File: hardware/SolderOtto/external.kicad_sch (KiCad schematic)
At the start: 13 parts, among them J901 Conn_01x08

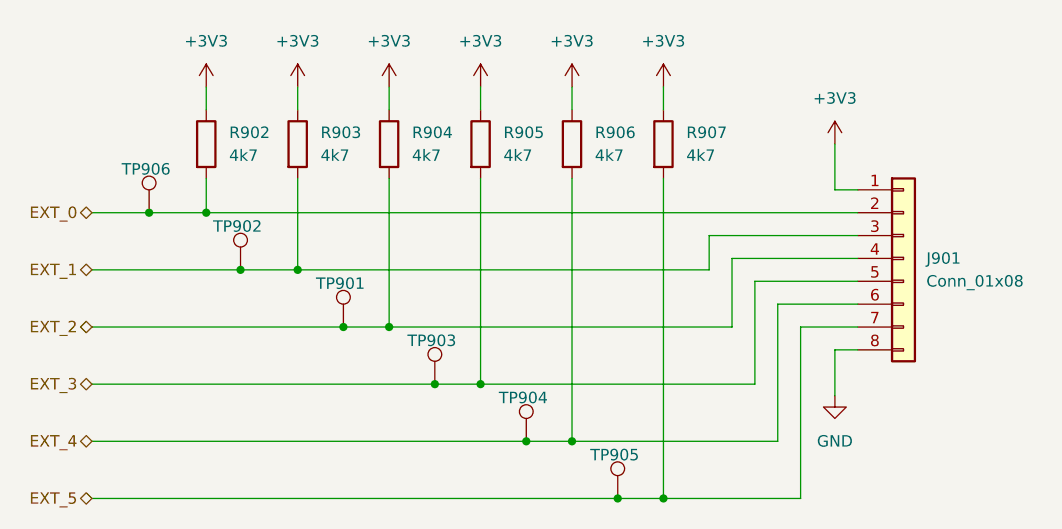
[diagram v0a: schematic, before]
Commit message: create adapter to enclosure for display
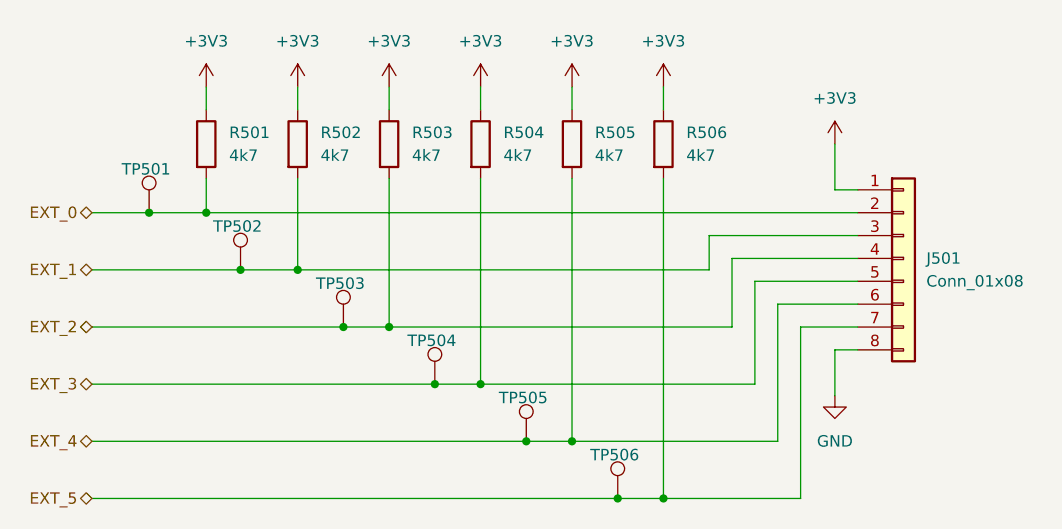
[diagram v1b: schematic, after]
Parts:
- renumbered J901 to J501, R902 to R501, R903 to R502, R904 to R503, R905 to R504, R906 to R505, R907 to R506, TP906 to TP501, TP902 to TP502, TP901 to TP503, TP903 to TP504, TP904 to TP505, TP905 to TP506
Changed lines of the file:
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@@
 		(dnp no)
 		(fields_autoplaced yes)
-		(property "Reference" "R907"
+		(property "Reference" "R506"
 			(at 135.89 40.6399 0)
 			(effects
@@
 			(project "SolderOtto"
 				(path "/04e99464-bf33-4a4f-8397-d26b5ec904f3/cd418f0e-1056-4277-8df0-d16a810128a6"
-					(reference "R907")
+					(reference "R506")
 					(unit 1)
 				)
@@
 		(dnp no)
 		(fields_autoplaced yes)
-		(property "Reference" "#PWR0909"
+		(property "Reference" "#PWR0505"
 			(at 123.19 39.37 0)
 			(effects
@@
 			(project "SolderOtto"
 				(path "/04e99464-bf33-4a4f-8397-d26b5ec904f3/cd418f0e-1056-4277-8df0-d16a810128a6"
-					(reference "#PWR0909")
+					(reference "#PWR0505")
 					(unit 1)
 				)
@@
 		(dnp no)
 		(fields_autoplaced yes)
-		(property "Reference" "R906"
+		(property "Reference" "R505"
 			(at 125.73 40.6399 0)
 			(effects
@@
 			(project "SolderOtto"
 				(path "/04e99464-bf33-4a4f-8397-d26b5ec904f3/cd418f0e-1056-4277-8df0-d16a810128a6"
-					(reference "R906")
+					(reference "R505")
 					(unit 1)
 				)
@@
 		(dnp no)
 		(fields_autoplaced yes)
-		(property "Reference" "R902"
+		(property "Reference" "R501"
 			(at 85.09 40.6399 0)
 			(effects
@@
 			(project "SolderOtto"
 				(path "/04e99464-bf33-4a4f-8397-d26b5ec904f3/cd418f0e-1056-4277-8df0-d16a810128a6"
-					(reference "R902")
+					(reference "R501")
 					(unit 1)
 				)
@@
 		(dnp no)
 		(fields_autoplaced yes)
-		(property "Reference" "#PWR0905"
+		(property "Reference" "#PWR0501"
 			(at 82.55 39.37 0)
 			(effects
@@
 			(project "SolderOtto"
 				(path "/04e99464-bf33-4a4f-8397-d26b5ec904f3/cd418f0e-1056-4277-8df0-d16a810128a6"
-					(reference "#PWR0905")
+					(reference "#PWR0501")
 					(unit 1)
 				)
@@
 		(on_board yes)
 		(dnp no)
-		(property "Reference" "TP903"
+		(property "Reference" "TP504"
 			(at 104.902 63.754 0)
 			(effects
@@
 			(project "SolderOtto"
 				(path "/04e99464-bf33-4a4f-8397-d26b5ec904f3/cd418f0e-1056-4277-8df0-d16a810128a6"
-					(reference "TP903")
+					(reference "TP504")
 					(unit 1)
 				)
@@
 		(on_board yes)
 		(dnp no)
-		(property "Reference" "TP902"
+		(property "Reference" "TP502"
 			(at 83.312 51.054 0)
 			(effects
@@
 			(project "SolderOtto"
 				(path "/04e99464-bf33-4a4f-8397-d26b5ec904f3/cd418f0e-1056-4277-8df0-d16a810128a6"
-					(reference "TP902")
+					(reference "TP502")
 					(unit 1)
 				)
@@
 		(on_board yes)
 		(dnp no)
-		(property "Reference" "TP905"
+		(property "Reference" "TP506"
 			(at 125.222 76.454 0)
 			(effects
@@
 			(project "SolderOtto"
 				(path "/04e99464-bf33-4a4f-8397-d26b5ec904f3/cd418f0e-1056-4277-8df0-d16a810128a6"
-					(reference "TP905")
+					(reference "TP506")
 					(unit 1)
 				)
@@
 		(on_board yes)
 		(dnp no)
-		(property "Reference" "TP906"
+		(property "Reference" "TP501"
 			(at 73.152 44.704 0)
 			(effects
@@
 			(project "SolderOtto"
 				(path "/04e99464-bf33-4a4f-8397-d26b5ec904f3/cd418f0e-1056-4277-8df0-d16a810128a6"
-					(reference "TP906")
+					(reference "TP501")
 					(unit 1)
 				)
@@
 		(dnp no)
 		(fields_autoplaced yes)
-		(property "Reference" "#PWR0907"
+		(property "Reference" "#PWR0503"
 			(at 102.87 39.37 0)
 			(effects
@@
 			(project "SolderOtto"
 				(path "/04e99464-bf33-4a4f-8397-d26b5ec904f3/cd418f0e-1056-4277-8df0-d16a810128a6"
-					(reference "#PWR0907")
+					(reference "#PWR0503")
 					(unit 1)
 				)
@@
 		(dnp no)
 		(fields_autoplaced yes)
-		(property "Reference" "#PWR0908"
+		(property "Reference" "#PWR0504"
 			(at 113.03 39.37 0)
 			(effects
@@
 			(project "SolderOtto"
 				(path "/04e99464-bf33-4a4f-8397-d26b5ec904f3/cd418f0e-1056-4277-8df0-d16a810128a6"
-					(reference "#PWR0908")
+					(reference "#PWR0504")
 					(unit 1)
 				)
@@
 		(dnp no)
 		(fields_autoplaced yes)
-		(property "Reference" "#PWR0906"
+		(property "Reference" "#PWR0502"
 			(at 92.71 39.37 0)
 			(effects
@@
 			(project "SolderOtto"
 				(path "/04e99464-bf33-4a4f-8397-d26b5ec904f3/cd418f0e-1056-4277-8df0-d16a810128a6"
-					(reference "#PWR0906")
+					(reference "#PWR0502")
 					(unit 1)
 				)
@@
 		(dnp no)
 		(fields_autoplaced yes)
-		(property "Reference" "#PWR0911"
+		(property "Reference" "#PWR0507"
 			(at 152.4 45.72 0)
 			(effects
@@
 			(project "SolderOtto"
 				(path "/04e99464-bf33-4a4f-8397-d26b5ec904f3/cd418f0e-1056-4277-8df0-d16a810128a6"
-					(reference "#PWR0911")
+					(reference "#PWR0507")
 					(unit 1)
 				)
@@
 		(on_board yes)
 		(dnp no)
-		(property "Reference" "TP901"
+		(property "Reference" "TP503"
 			(at 94.742 57.404 0)
 			(effects
@@
 			(project "SolderOtto"
 				(path "/04e99464-bf33-4a4f-8397-d26b5ec904f3/cd418f0e-1056-4277-8df0-d16a810128a6"
-					(reference "TP901")
+					(reference "TP503")
 					(unit 1)
 				)
@@
 		(dnp no)
 		(fields_autoplaced yes)
-		(property "Reference" "J901"
+		(property "Reference" "J501"
 			(at 162.56 54.6099 0)
 			(effects
@@
 			(project ""
 				(path "/04e99464-bf33-4a4f-8397-d26b5ec904f3/cd418f0e-1056-4277-8df0-d16a810128a6"
-					(reference "J901")
+					(reference "J501")
 					(unit 1)
 				)
@@
 		(dnp no)
 		(fields_autoplaced yes)
-		(property "Reference" "R903"
+		(property "Reference" "R502"
 			(at 95.25 40.6399 0)
 			(effects
@@
 			(project "SolderOtto"
 				(path "/04e99464-bf33-4a4f-8397-d26b5ec904f3/cd418f0e-1056-4277-8df0-d16a810128a6"
-					(reference "R903")
+					(reference "R502")
 					(unit 1)
 				)
@@
 		(dnp no)
 		(fields_autoplaced yes)
-		(property "Reference" "R905"
+		(property "Reference" "R504"
 			(at 115.57 40.6399 0)
 			(effects
@@
 			(project "SolderOtto"
 				(path "/04e99464-bf33-4a4f-8397-d26b5ec904f3/cd418f0e-1056-4277-8df0-d16a810128a6"
-					(reference "R905")
+					(reference "R504")
 					(unit 1)
 				)
@@
 		(dnp no)
 		(fields_autoplaced yes)
-		(property "Reference" "R904"
+		(property "Reference" "R503"
 			(at 105.41 40.6399 0)
 			(effects
@@
 			(project "SolderOtto"
 				(path "/04e99464-bf33-4a4f-8397-d26b5ec904f3/cd418f0e-1056-4277-8df0-d16a810128a6"
-					(reference "R904")
+					(reference "R503")
 					(unit 1)
 				)
@@
 		(dnp no)
 		(fields_autoplaced yes)
-		(property "Reference" "#PWR0910"
+		(property "Reference" "#PWR0506"
 			(at 133.35 39.37 0)
 			(effects
@@
 			(project "SolderOtto"
 				(path "/04e99464-bf33-4a4f-8397-d26b5ec904f3/cd418f0e-1056-4277-8df0-d16a810128a6"
-					(reference "#PWR0910")
+					(reference "#PWR0506")
 					(unit 1)
 				)
@@
 		(on_board yes)
 		(dnp no)
-		(property "Reference" "TP904"
+		(property "Reference" "TP505"
 			(at 115.062 70.104 0)
 			(effects
@@
 			(project "SolderOtto"
 				(path "/04e99464-bf33-4a4f-8397-d26b5ec904f3/cd418f0e-1056-4277-8df0-d16a810128a6"
-					(reference "TP904")
+					(reference "TP505")
 					(unit 1)
 				)
@@
 		(dnp no)
 		(fields_autoplaced yes)
-		(property "Reference" "#PWR0912"
+		(property "Reference" "#PWR0508"
 			(at 152.4 76.2 0)
 			(effects
@@
 			(project "SolderOtto"
 				(path "/04e99464-bf33-4a4f-8397-d26b5ec904f3/cd418f0e-1056-4277-8df0-d16a810128a6"
-					(reference "#PWR0912")
-					(unit 1)
-				)
+					(reference "#PWR0508")
+					(unit 1)
+				)

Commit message: save work
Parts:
- TP501: value ZCD -> EXT0
- TP502: value ZCD -> EXT1
- TP503: value ZCD -> EXT2
- TP504: value ZCD -> EXT3
- TP505: value ZCD -> EXT4
- TP506: value ZCD -> EXT5
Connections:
- net EXT_3: now also J501.6 (Pin_6); no longer J501.5 (Pin_5)
- net EXT_4: now also J501.7 (Pin_7); no longer J501.6 (Pin_6)
- net EXT_5: now also J501.8 (Pin_8); no longer J501.7 (Pin_7)
- net GND: now also J501.5 (Pin_5); no longer J501.8 (Pin_8)
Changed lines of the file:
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@@
 	(wire
 		(pts
-			(xy 123.19 74.93) (xy 146.05 74.93)
-		)
-		(stroke
-			(width 0)
-			(type default)
-		)
-	)
-	(wire
-		(pts
-			(xy 152.4 69.85) (xy 152.4 64.77)
+			(xy 152.4 64.77) (xy 154.94 64.77)
+		)
+		(stroke
+			(width 0)
+			(type default)
+		)
+	)
+	(wire
+		(pts
+			(xy 123.19 74.93) (xy 149.86 74.93)
+		)
+		(stroke
+			(width 0)
+			(type default)
+		)
+	)
+	(wire
+		(pts
+			(xy 143.51 62.23) (xy 143.51 57.15)
 		)
 		(stroke
@@
 	(wire
 		(pts
-			(xy 148.59 81.28) (xy 148.59 62.23)
-		)
-		(stroke
-			(width 0)
-			(type default)
-		)
-	)
-	(wire
-		(pts
 			(xy 102.87 62.23) (xy 140.97 62.23)
 		)
@@
 	(wire
 		(pts
-			(xy 143.51 68.58) (xy 143.51 57.15)
+			(xy 147.32 68.58) (xy 147.32 59.69)
 		)
 		(stroke
@@
 	(wire
 		(pts
-			(xy 146.05 59.69) (xy 146.05 74.93)
-		)
-		(stroke
-			(width 0)
-			(type default)
-		)
-	)
-	(wire
-		(pts
-			(xy 133.35 81.28) (xy 148.59 81.28)
+			(xy 152.4 81.28) (xy 152.4 64.77)
+		)
+		(stroke
+			(width 0)
+			(type default)
+		)
+	)
+	(wire
+		(pts
+			(xy 149.86 62.23) (xy 149.86 74.93)
+		)
+		(stroke
+			(width 0)
+			(type default)
+		)
+	)
+	(wire
+		(pts
+			(xy 133.35 81.28) (xy 152.4 81.28)
 		)
 		(stroke
@@
 	(wire
 		(pts
-			(xy 152.4 64.77) (xy 154.94 64.77)
-		)
-		(stroke
-			(width 0)
-			(type default)
-		)
-	)
-	(wire
-		(pts
-			(xy 154.94 59.69) (xy 146.05 59.69)
+			(xy 143.51 57.15) (xy 154.94 57.15)
+		)
+		(stroke
+			(width 0)
+			(type default)
+		)
+	)
+	(wire
+		(pts
+			(xy 154.94 62.23) (xy 149.86 62.23)
 		)
 		(stroke
@@
 	(wire
 		(pts
-			(xy 113.03 68.58) (xy 143.51 68.58)
+			(xy 113.03 68.58) (xy 147.32 68.58)
 		)
 		(stroke
@@
 	(wire
 		(pts
-			(xy 148.59 62.23) (xy 154.94 62.23)
-		)
-		(stroke
-			(width 0)
-			(type default)
-		)
-	)
-	(wire
-		(pts
 			(xy 133.35 81.28) (xy 133.35 45.72)
 		)
@@
 	(wire
 		(pts
-			(xy 143.51 57.15) (xy 154.94 57.15)
+			(xy 147.32 59.69) (xy 154.94 59.69)
 		)
 		(stroke
@@
 			)
 		)
-		(property "Value" "ZCD"
+		(property "Value" "EXT3"
 			(at 110.49 66.5479 0)
 			(effects
@@
 			)
 		)
-		(property "Value" "ZCD"
+		(property "Value" "EXT1"
 			(at 88.9 53.8479 0)
 			(effects
@@
 			)
 		)
-		(property "Value" "ZCD"
+		(property "Value" "EXT5"
 			(at 130.81 79.2479 0)
 			(effects
@@
 			)
 		)
-		(property "Value" "ZCD"
+		(property "Value" "EXT0"
 			(at 78.74 47.4979 0)
 			(effects
@@
 			)
 		)
-		(property "Value" "ZCD"
+		(property "Value" "EXT2"
 			(at 100.33 60.1979 0)
 			(effects
@@
 			)
 		)
-		(property "Value" "ZCD"
+		(property "Value" "EXT4"
 			(at 120.65 72.8979 0)
 			(effects
@@
 	(symbol
 		(lib_id "power:GND")
-		(at 152.4 69.85 0)
+		(at 143.51 62.23 0)
 		(unit 1)
 		(exclude_from_sim no)
@@
 		(fields_autoplaced yes)
 		(property "Reference" "#PWR0508"
-			(at 152.4 76.2 0)
+			(at 143.51 68.58 0)
 			(effects
 				(font
@@
 		)
 		(property "Value" "GND"
-			(at 152.4 74.93 0)
+			(at 143.51 67.31 0)
 			(effects
 				(font
@@
 		)
 		(property "Footprint" ""
-			(at 152.4 69.85 0)
+			(at 143.51 62.23 0)
 			(effects
 				(font
@@
 		)
 		(property "Datasheet" ""
-			(at 152.4 69.85 0)
+			(at 143.51 62.23 0)
 			(effects
 				(font
@@
 		)
 		(property "Description" "Power symbol creates a global label with name \"GND\" , ground"
-			(at 152.4 69.85 0)
-			(effects
-				(font
+			(at 143.51 62.23 0)
+			(effects
+				(font

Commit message: save work
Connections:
- net EXT_0: now also J501.8 (Pin_8), R506.2, TP506.1; no longer J501.2 (Pin_2), R501.2, TP501.1
- net EXT_1: now also J501.7 (Pin_7), R505.2, TP505.1; no longer J501.3 (Pin_3), R502.2, TP502.1
- net EXT_2: now also J501.6 (Pin_6), R504.2, TP504.1; no longer J501.4 (Pin_4), R503.2, TP503.1
- net EXT_3: now also J501.4 (Pin_4), R503.2, TP503.1; no longer J501.6 (Pin_6), R504.2, TP504.1
- net EXT_4: now also J501.3 (Pin_3), R502.2, TP502.1; no longer J501.7 (Pin_7), R505.2, TP505.1
- net EXT_5: now also J501.2 (Pin_2), R501.2, TP501.1; no longer J501.8 (Pin_8), R506.2, TP506.1
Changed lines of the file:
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@@
 	(hierarchical_label "EXT_0"
+		(shape bidirectional)
+		(at 69.85 81.28 180)
+		(fields_autoplaced yes)
+		(effects
+			(font
+				(size 1.27 1.27)
+			)
+			(justify right)
+		)
+	)
+	(hierarchical_label "EXT_2"
+		(shape bidirectional)
+		(at 69.85 68.58 180)
+		(fields_autoplaced yes)
+		(effects
+			(font
+				(size 1.27 1.27)
+			)
+			(justify right)
+		)
+	)
+	(hierarchical_label "EXT_4"
+		(shape bidirectional)
+		(at 69.85 55.88 180)
+		(fields_autoplaced yes)
+		(effects
+			(font
+				(size 1.27 1.27)
+			)
+			(justify right)
+		)
+	)
+	(hierarchical_label "EXT_1"
+		(shape bidirectional)
+		(at 69.85 74.93 180)
+		(fields_autoplaced yes)
+		(effects
+			(font
+				(size 1.27 1.27)
+			)
+			(justify right)
+		)
+	)
+	(hierarchical_label "EXT_5"
 		(shape bidirectional)
 		(at 69.85 49.53 180)
@@
 		)
 	)
-	(hierarchical_label "EXT_2"
+	(hierarchical_label "EXT_3"
 		(shape bidirectional)
 		(at 69.85 62.23 180)
 		(fields_autoplaced yes)
 		(effects
-			(font
-				(size 1.27 1.27)
-			)
-			(justify right)
-		)
-	)
-	(hierarchical_label "EXT_4"
-		(shape bidirectional)
-		(at 69.85 74.93 180)
-		(fields_autoplaced yes)
-		(effects
-			(font
-				(size 1.27 1.27)
-			)
-			(justify right)
-		)
-	)
-	(hierarchical_label "EXT_1"
-		(shape bidirectional)
-		(at 69.85 55.88 180)
-		(fields_autoplaced yes)
-		(effects
-			(font
-				(size 1.27 1.27)
-			)
-			(justify right)
-		)
-	)
-	(hierarchical_label "EXT_5"
-		(shape bidirectional)
-		(at 69.85 81.28 180)
-		(fields_autoplaced yes)
-		(effects
-			(font
-				(size 1.27 1.27)
-			)
-			(justify right)
-		)
-	)
-	(hierarchical_label "EXT_3"
-		(shape bidirectional)
-		(at 69.85 68.58 180)
-		(fields_autoplaced yes)
-		(effects

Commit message: fix some part numbers
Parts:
- J501: Digikey (none) -> WM16881-ND;WM16864CT-ND;WM14964-ND;WM15189-ND
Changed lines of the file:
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@@
+			)
+		)
+		(property "Digikey" "WM16881-ND;WM16864CT-ND;WM14964-ND;WM15189-ND"
+			(at 160.02 54.61 0)
+			(effects
+				(font
+					(size 1.27 1.27)
+				)
+				(hide yes)
 			)
 		)

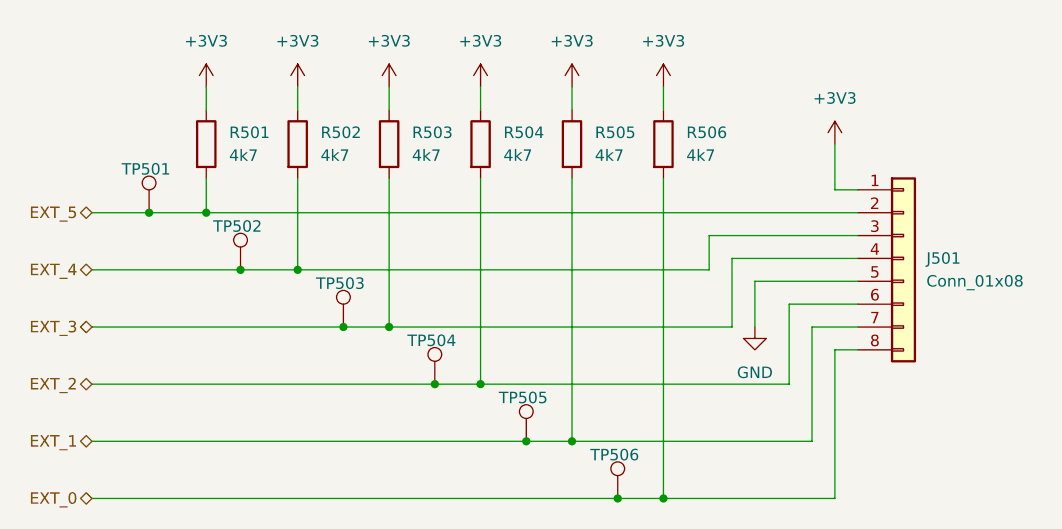
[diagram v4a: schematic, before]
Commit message: rework pcb due to not working one
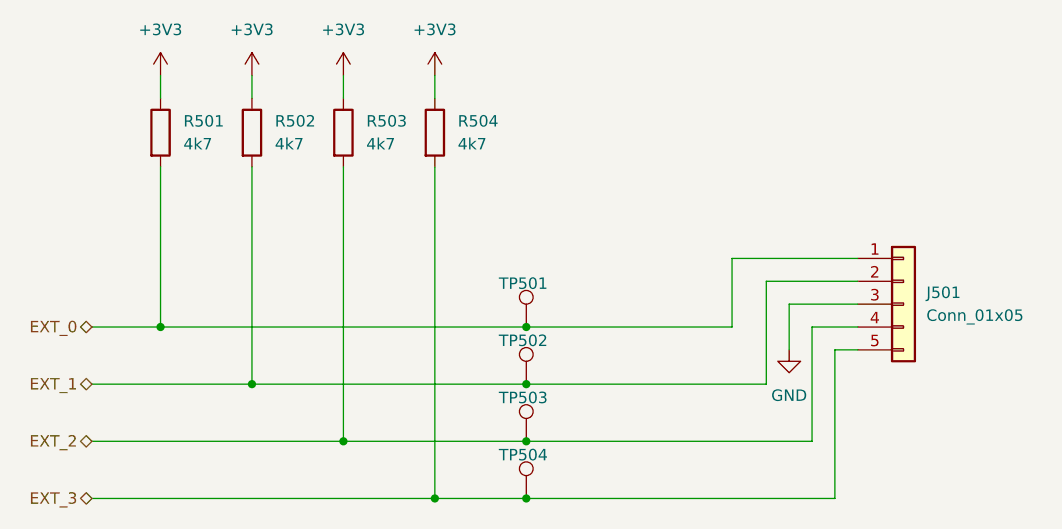
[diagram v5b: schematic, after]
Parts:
- removed J501: Conn_01x08, Connector_Molex:Molex_Nano-Fit_105310-xx08_2x04_P2.50mm_Vertical, symbol Connector_Generic:Conn_01x08
- removed R501, R502: 4k7, Resistor_SMD:R_0603_1608Metric, symbol Device:R
- removed TP501: EXT0, TestPoint:TestPoint_Keystone_5015_Micro-Minature, symbol Connector:TestPoint
- removed TP502: EXT1, TestPoint:TestPoint_Keystone_5015_Micro-Minature, symbol Connector:TestPoint
- added J501: Conn_01x05, Connector_Molex:Molex_Nano-Fit_105309-xx05_1x05_P2.50mm_Vertical, symbol Connector_Generic:Conn_01x05
- renumbered R506 to R501, R505 to R502, R504 to R503, R503 to R504, TP503 to TP501, TP504 to TP502, TP505 to TP503, TP506 to TP504
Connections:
- net EXT_0: now also TP501.1, J501.1 (Pin_1); no longer TP504.1
- net EXT_1: now also TP502.1, J501.2 (Pin_2); no longer TP503.1
- net EXT_2: now also TP503.1, J501.4 (Pin_4); no longer TP502.1
- net EXT_3: now also TP504.1, J501.5 (Pin_5); no longer TP501.1
- net GND: now also J501.3 (Pin_3)
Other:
- moved on the sheet: R501, R502, R503, R504, TP501, TP502, TP504

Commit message: rework pcb
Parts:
- J501: Digikey (none) -> WM16868-ND
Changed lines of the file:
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@@
 			)
 		)
-		(property "Datasheet" "~"
+		(property "Datasheet" "https://www.digikey.de/de/products/detail/molex/1053091105/7693149"
 			(at 160.02 59.69 0)
 			(effects
@@
 			(at 160.02 59.69 0)
 			(effects
+				(font
+					(size 1.27 1.27)
+				)
+				(hide yes)
+			)
+		)
+		(property "Digikey" "WM16868-ND"
+			(at 160.02 59.69 0)
+			(effects
